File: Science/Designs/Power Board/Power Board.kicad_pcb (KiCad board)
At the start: 2 copper layers, 114.3 x 93.7 mm, 29 parts, among them P1 PWR_IN, P2 MOTOR_PWR_OUT, P3 MAIN_PWR_OUT, P4 I2C, P5 MOTOR_SW, P6 REG_12V, P7 REG_5V, U1 INA219, U2 INA219, U3 INA219

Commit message: Almost done
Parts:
- moved REF** 28.9 mm to (78.7, 29.5)
- moved P1 15.2 mm to (100.6, 55.4), turned to 270 degrees
- moved P5 2.17 mm to (141.7, 92.2)
- moved R3 1.78 mm to (137.2, 64.0)
- moved R5 1.30 mm to (156.5, 82.5)
- moved R4 1.05 mm to (115.3, 62.0)
- moved P2 0.61 mm to (98.0, 92.0)
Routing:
- net Net-(P5-Pad1): track 73.2 -> 139.9 mm, vias 3 -> 60
- net +24V: track 151.7 -> 108.8 mm, vias 3 -> 5
- net GND: track 37.1 -> 39.2 mm
- net Net-(P2-Pad4): track 49.8 -> 51.3 mm
- net /24V_IN: track 2.73 -> 2.03 mm
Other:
- board text added: "+24V Power Input"

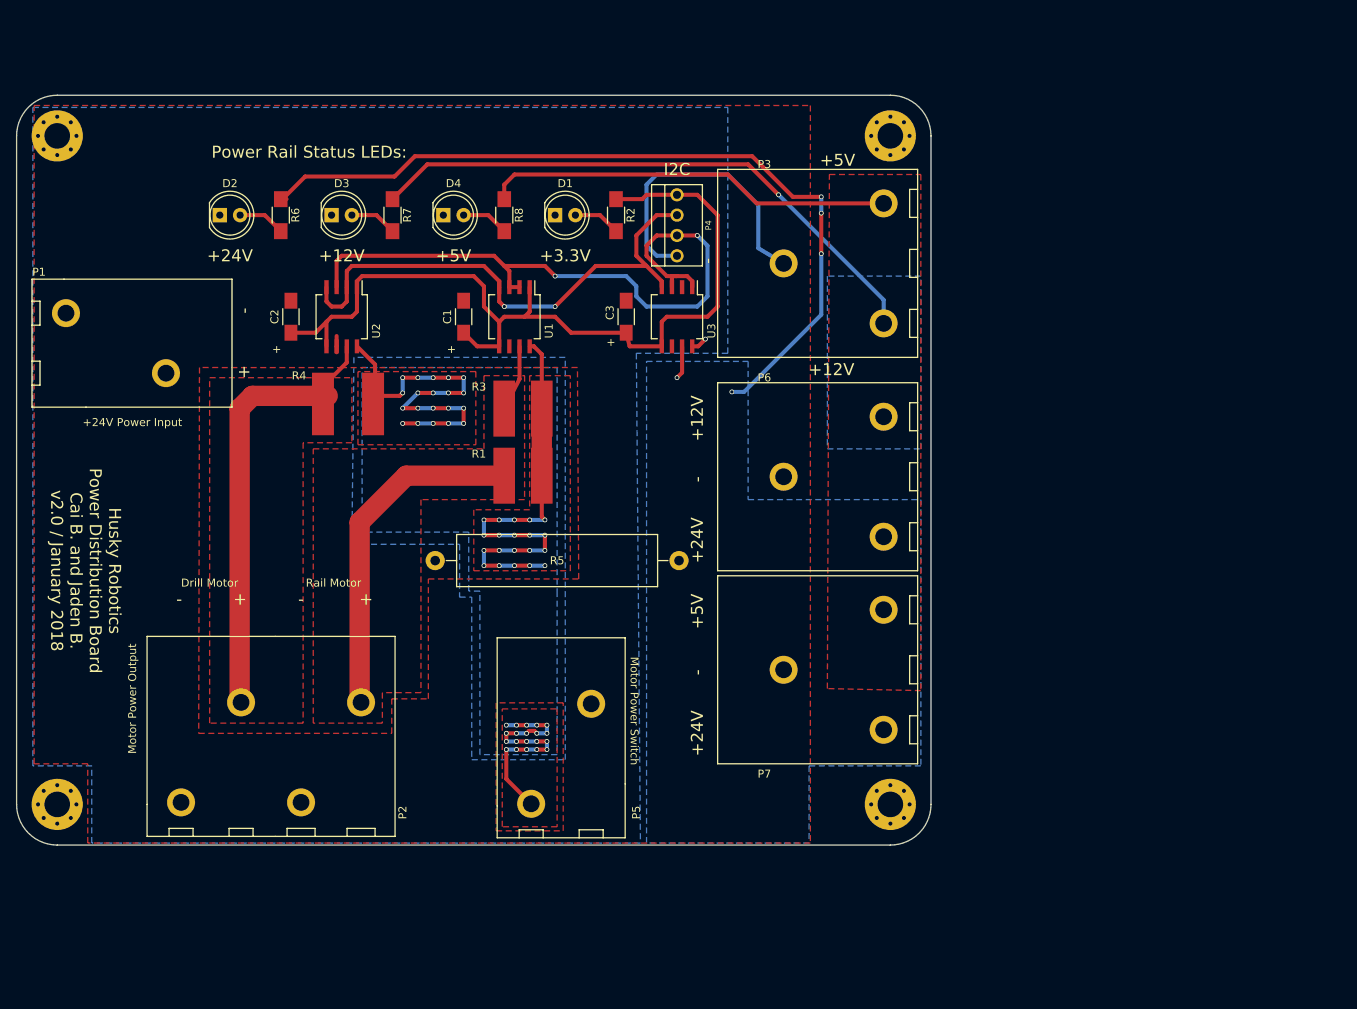
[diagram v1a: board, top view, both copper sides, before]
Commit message: Redesign started. Looks better, although still has issues
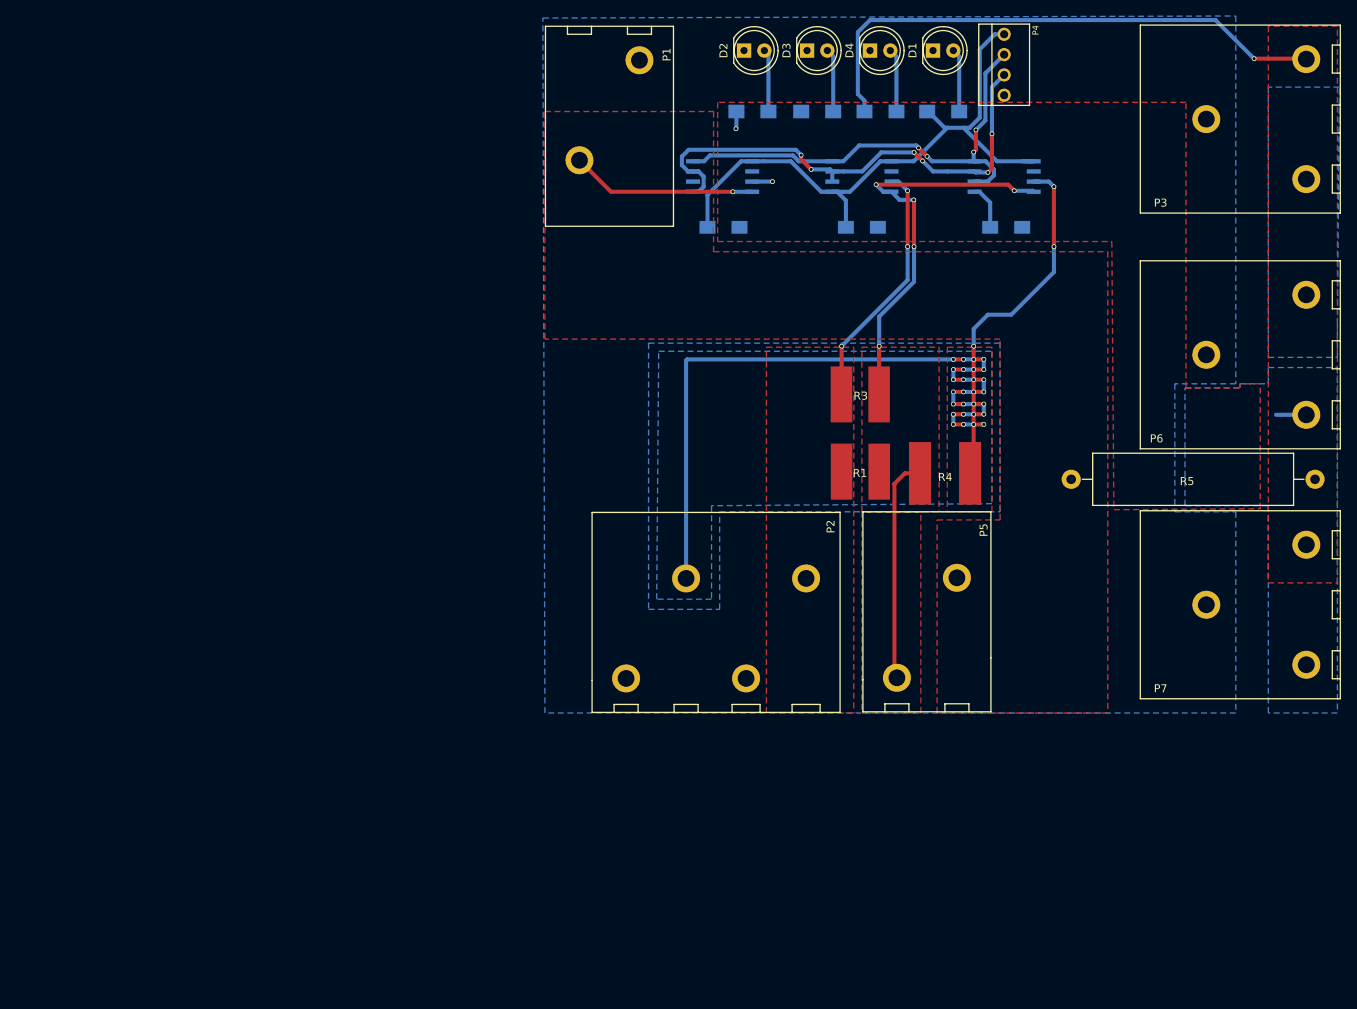
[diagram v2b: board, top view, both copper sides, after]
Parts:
- removed REF** (x4): MountingHole_3.2mm_M3_Pad_Via, Mounting_Holes:MountingHole_3.2mm_M3_Pad_Via
- C1, C2, C3, R2, R6, R7, R8: moved to B.Cu
- U1, U2, U3: footprint ScienceFootprints:SO-8_5.3x6.2mm_Pitch1.27mm -> Housings_SOIC:SO-8_5.3x6.2mm_Pitch1.27mm; moved to B.Cu
- moved U2 84.6 mm to (197.1, 34.5), turned to 0 degrees
- moved R5 80.1 mm to (236.0, 72.4)
- moved R4 74.9 mm to (189.5, 72.6), turned to 0 degrees
- moved C1 68.7 mm to (197.4, 40.9), turned to 0 degrees
- moved D2 68.7 mm to (164.6, 18.8)
- moved D3 62.9 mm to (172.5, 18.8)
- moved R6 60.4 mm to (165.6, 26.4), turned to 0 degrees
- moved P2 57.7 mm to (153.6, 76.5)
- moved D4 57.2 mm to (180.3, 18.8)
- moved P3 55.8 mm to (214.1, 39.1)
- moved C2 55.2 mm to (162.0, 40.9), turned to 0 degrees
- moved P6 55.0 mm to (214.1, 68.6)
- moved R7 54.6 mm to (173.7, 26.4), turned to 0 degrees
- moved P7 53.5 mm to (214.1, 99.8)
- moved D1 51.5 mm to (188.2, 18.8)
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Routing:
- net +24V: track 108.8 -> 8.52 mm, vias 5 -> 2
- net Net-(P2-Pad2): track 55.1 -> 141.2 mm, vias 0 -> 31
- net +12V: track 73.1 -> 0.00 mm, vias 1 -> 0
- net Net-(P5-Pad1): track 139.9 -> 79.8 mm, vias 60 -> 5
- net GND: track 39.2 -> 0.00 mm
- net +3V3: track 110.0 -> 84.0 mm
- net /I2C_SDA: track 85.6 -> 63.6 mm, vias 2 -> 6
- net /24V_IN: track 2.03 -> 23.2 mm
- net Net-(P2-Pad4): track 51.3 -> 31.4 mm, vias 0 -> 3
- net +5V: track 51.5 -> 69.0 mm, vias 0 -> 1
- net /I2C_SCL: track 66.7 -> 59.9 mm, vias 2 -> 4
- net Net-(D4-Pad2): track 5.91 -> 7.94 mm
- net Net-(D1-Pad2): track 5.91 -> 7.92 mm
- net Net-(D3-Pad2): track 5.91 -> 7.92 mm
- net Net-(D2-Pad2): track 5.91 -> 7.83 mm
- added copper zone on F.Cu, net +12V
- added copper zone on F.Cu, net /24V_IN
- added copper zone on B.Cu, net GND
- added copper zone on B.Cu, net Net-(P2-Pad2)
- removed copper zone on B.Cu, net /24V_IN
- removed copper zone on F.Cu, net GND
- removed copper zone on B.Cu, net Net-(P5-Pad1)
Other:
- board outline removed
- board text removed: "+"
- board text removed: "+12V"
- board text removed: "+24V"
- board text removed: "+24V Power Input"
- board text removed: "+3.3V"
- board text removed: "+5V"
- board text removed: "-"
- board text removed: "Drill Motor"
- board text removed: "Husky Robotics Power Distribution Board Cai B. and Jaden B. v2.0 / January 2018"
- board text removed: "I2C"
- board text removed: "Motor Power Output"
- board text removed: "Motor Power Switch"
- board text removed: "Power Rail Status LEDs:"
- board text removed: "Rail Motor"

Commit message: All connections made
I think I am within spec as much as I can be. Maybe we should go with 2oz copper on this board
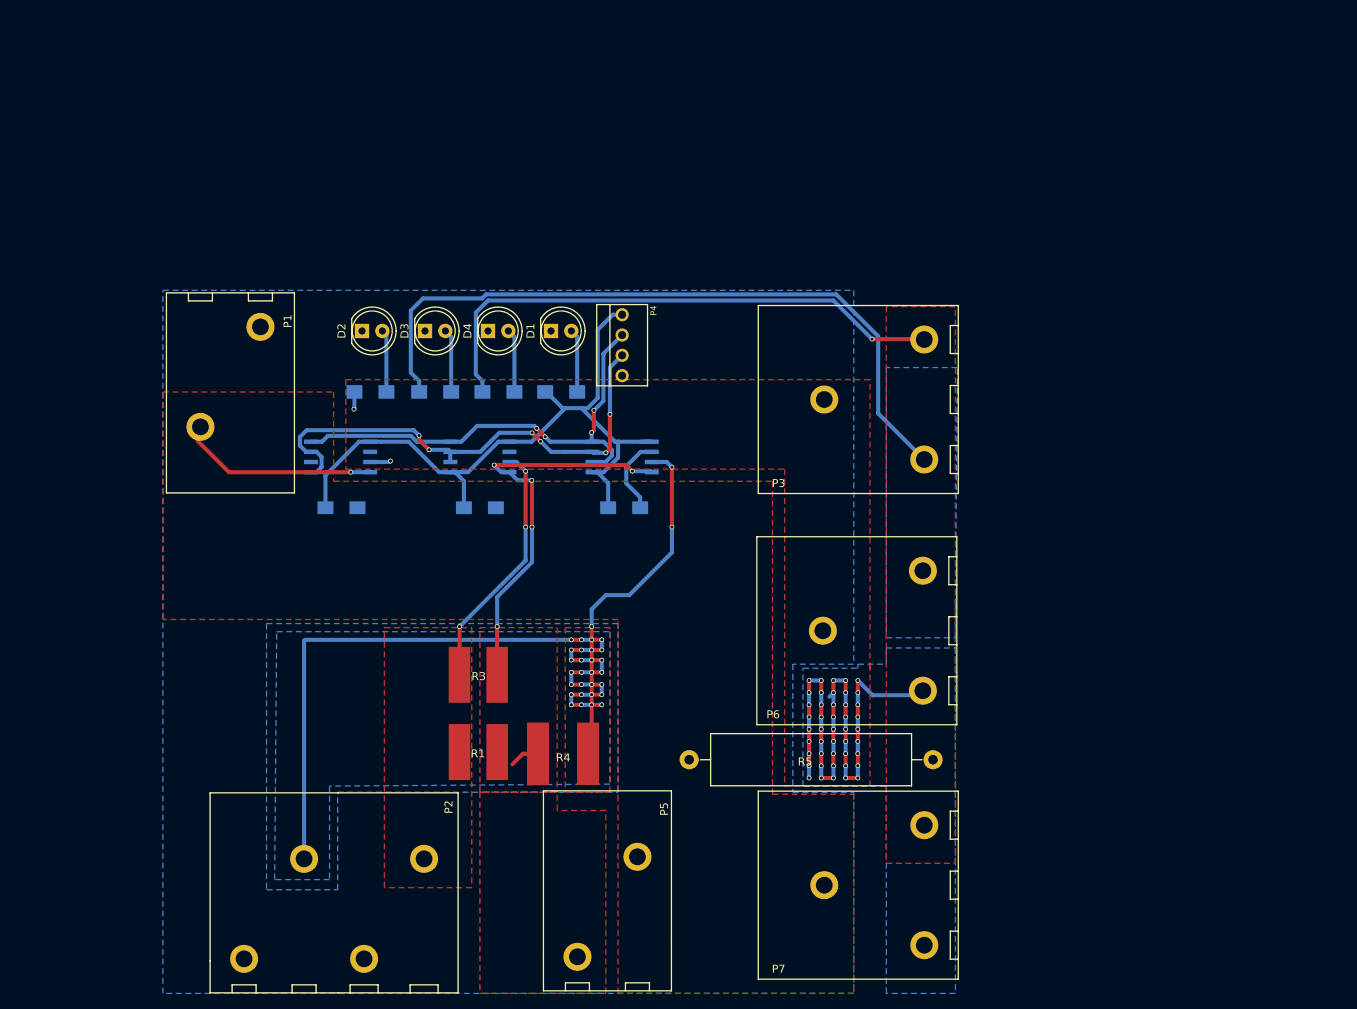
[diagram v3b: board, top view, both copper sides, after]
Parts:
- moved C1 59.2 mm to (149.6, 75.9)
- moved C2 59.2 mm to (114.3, 75.9)
- moved C3 59.2 mm to (131.6, 75.9)
- moved D1 59.2 mm to (140.5, 53.8)
- moved D2 59.2 mm to (116.8, 53.8)
- moved D3 59.2 mm to (124.7, 53.8)
- moved D4 59.2 mm to (132.6, 53.8)
- moved P2 59.2 mm to (105.8, 111.6)
- moved P3 59.2 mm to (166.4, 74.2)
- moved R2 59.2 mm to (141.7, 61.5)
- moved R3 59.2 mm to (131.6, 97.3)
- moved R8 59.2 mm to (133.9, 61.5)
- moved U1 59.2 mm to (131.6, 69.6)
- moved U2 59.2 mm to (149.4, 69.6)
- moved R7 59.2 mm to (126.0, 61.5)
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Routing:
- net +12V: track 0.00 -> 89.8 mm
- net +24V: track 8.52 -> 83.2 mm, vias 2 -> 47
- net Net-(P5-Pad1): track 79.8 -> 55.4 mm
- net GND: track 0.00 -> 9.83 mm
- net +3V3: track 84.0 -> 89.9 mm
- added copper zone on F.Cu, net +24V
- removed copper zone on F.Cu, net +12V

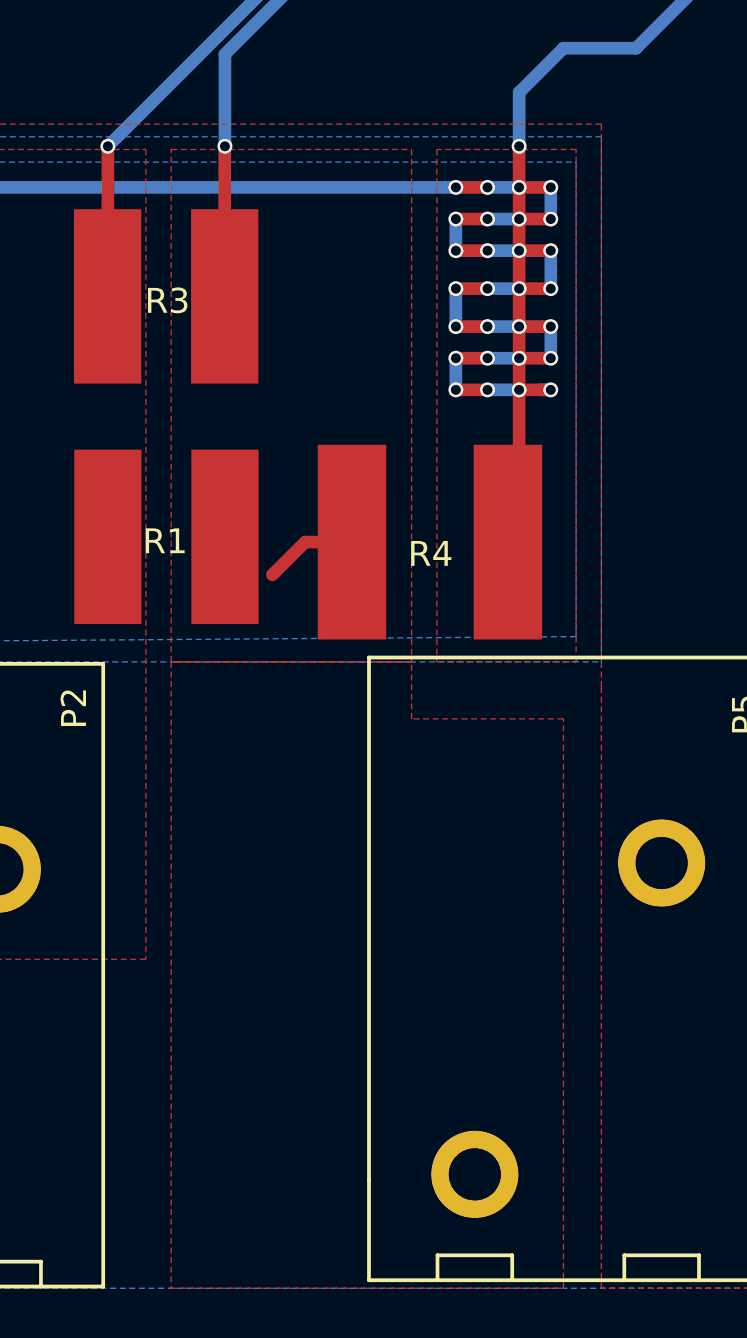
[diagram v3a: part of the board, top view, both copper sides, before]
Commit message: Fixed polygon combination
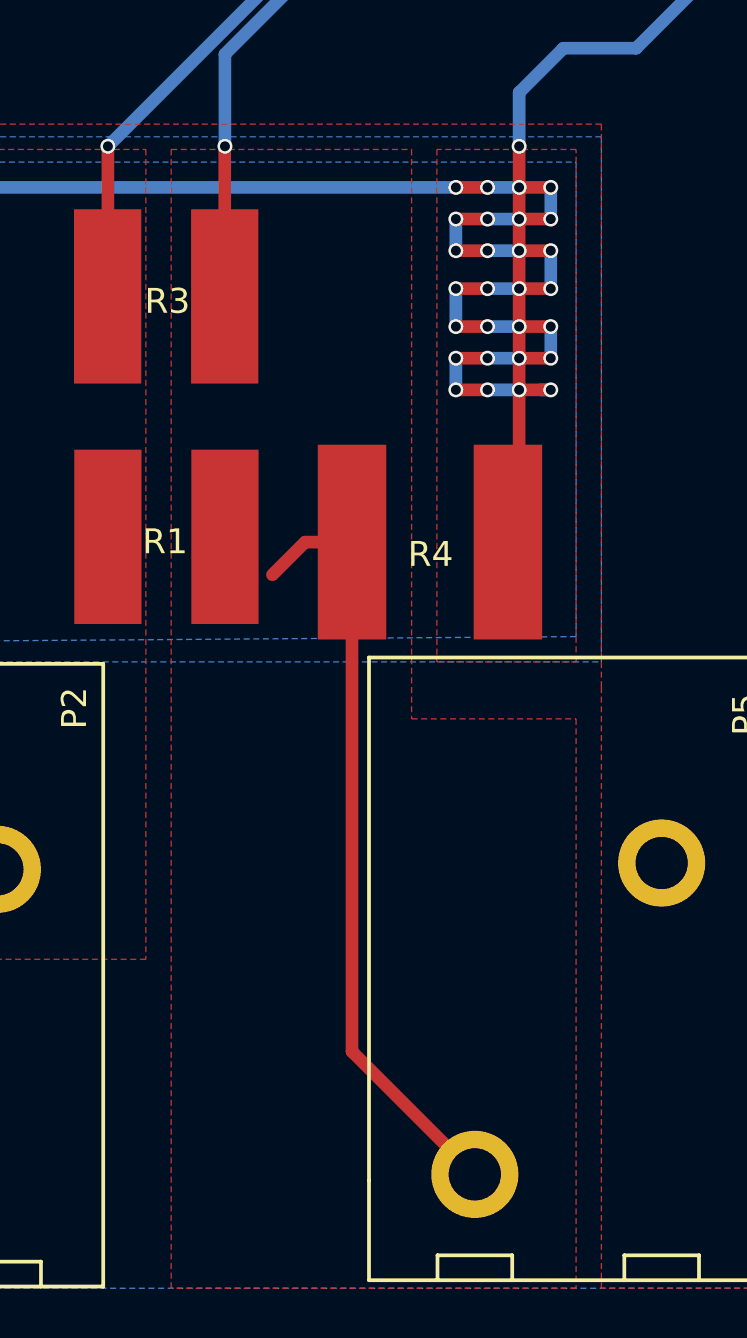
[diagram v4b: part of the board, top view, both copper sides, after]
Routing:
- net Net-(P5-Pad1): track 55.4 -> 82.9 mm
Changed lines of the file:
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@@
     (thickness 1.6)
     (drawings 0)
-    (tracks 345)
+    (tracks 347)
     (zones 0)
     (modules 25)
@@
   (segment (start 112.568001 66.961999) (end 111.839 67.691) (width 0.508) (layer B.Cu) (net 13))
   (segment (start 111.839 67.691) (end 110.456 67.691) (width 0.508) (layer B.Cu) (net 13))
+  (segment (start 143.764 132.08) (end 138.832 127.148) (width 0.508) (layer F.Cu) (net 14))
+  (segment (start 138.832 127.148) (end 138.832 106.696) (width 0.508) (layer F.Cu) (net 14))
   (segment (start 138.049 72.517) (end 136.288 72.517) (width 0.508) (layer B.Cu) (net 14))
   (segment (start 136.288 72.517) (end 135.272 71.501) (width 0.508) (layer B.Cu) (net 14))
@@
     (polygon
       (pts
-        (xy 131.572 90.932) (xy 141.224 90.932) (xy 141.224 111.506) (xy 131.572 111.506)
+        (xy 131.572 90.932) (xy 141.224 90.932) (xy 141.224 113.792) (xy 147.828 113.792) (xy 147.828 136.652)
+        (xy 131.572 136.652)
       )
     )
-  )
-  (zone (net 14) (net_name "Net-(P5-Pad1)") (layer F.Cu) (hatch edge 0.508)
-    (connect_pads (clearance 0.508))
-    (min_thickness 0.254)
-    (fill yes (arc_segments 16) (thermal_gap 0.508) (thermal_bridge_width 7))
-    (polygon
-      (pts
-        (xy 131.826 111.506) (xy 131.572 111.506) (xy 131.572 136.652) (xy 147.32 136.652) (xy 147.32 113.792)
-        (xy 141.224 113.792) (xy 141.224 111.506)
-      )
-    )

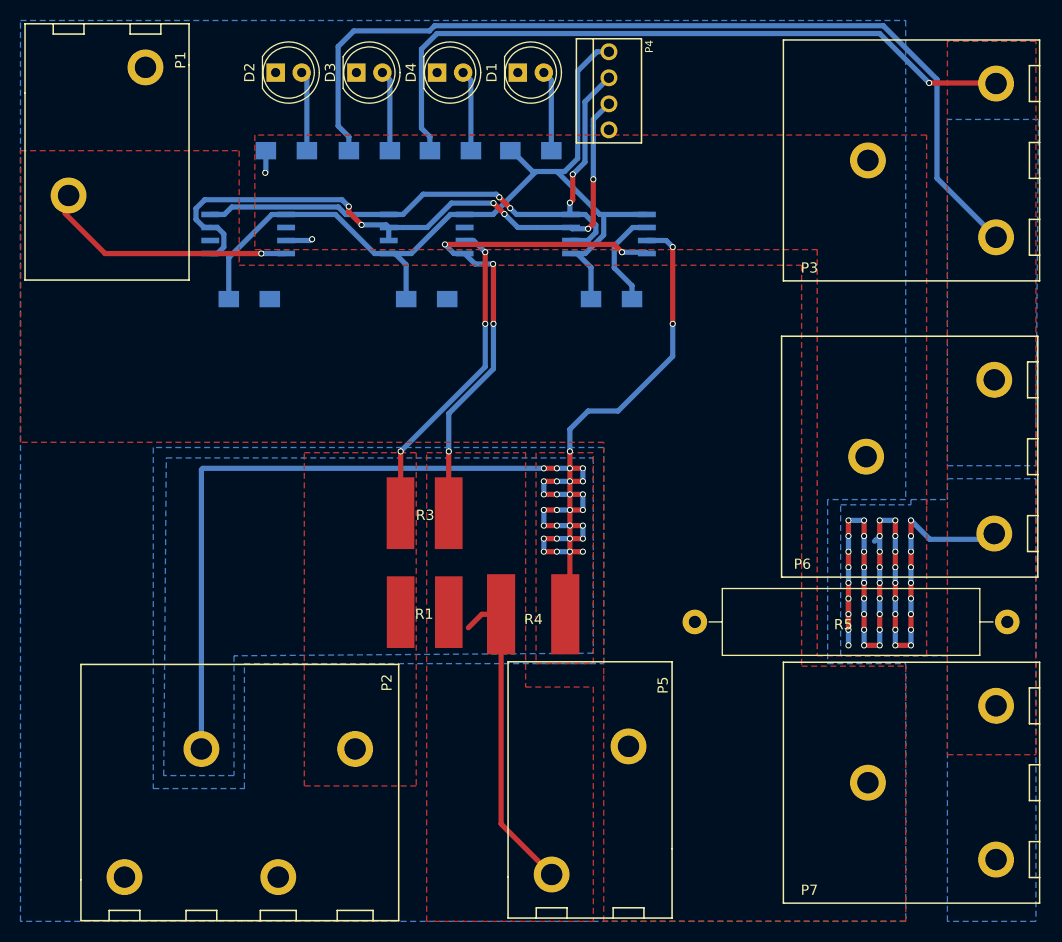
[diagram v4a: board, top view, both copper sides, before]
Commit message: Last trace changes
Will work on solder mask now
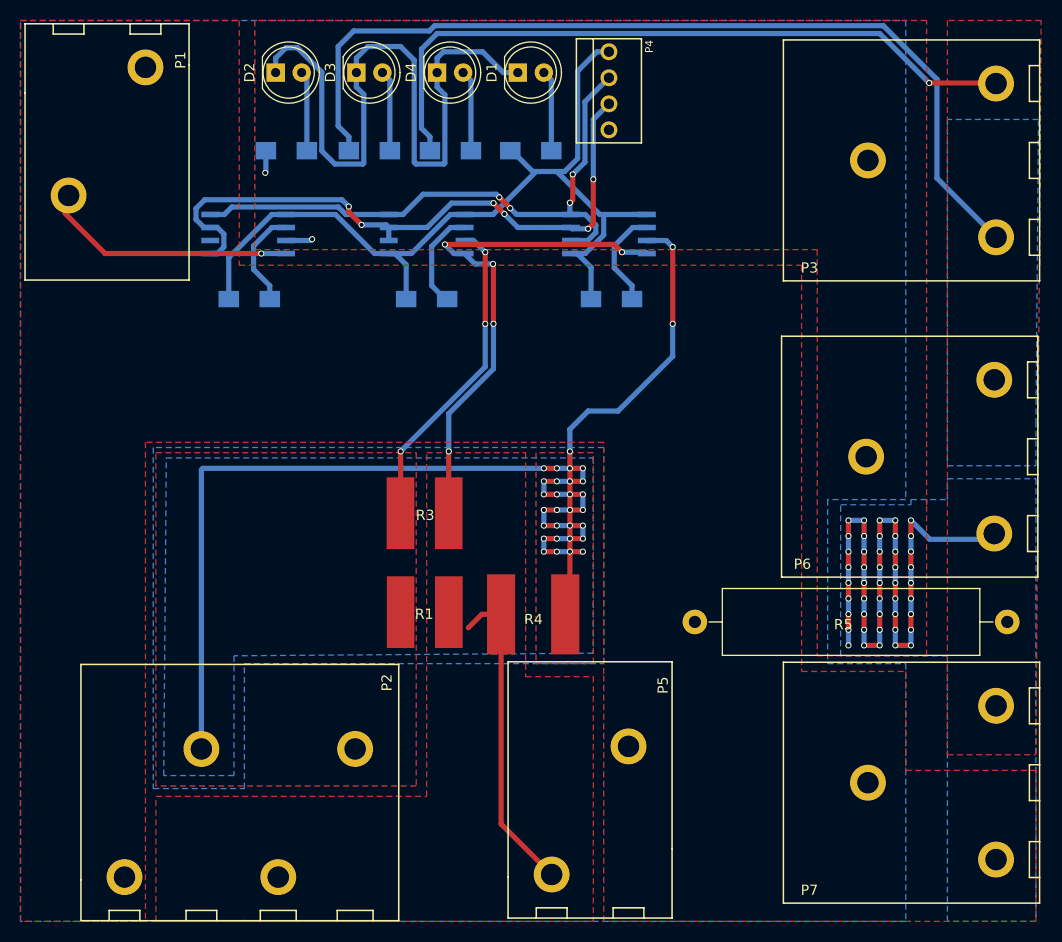
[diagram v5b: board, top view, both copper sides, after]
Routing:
- net GND: track 9.83 -> 98.9 mm
- net +24V: track 83.2 -> 80.9 mm
